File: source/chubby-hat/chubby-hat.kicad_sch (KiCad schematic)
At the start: 29 parts, among them J10 Conn_ARM_JTAG_SWD_10, J11 Conn_ARM_JTAG_SWD_10, J12 TC2030, J13 5V, J14 5V, J15 5V, J16 5V, J9 UART, SW1 RUN, SW2 BOOT, U1 AMS1117-3.3, U2 RP2040-Zero

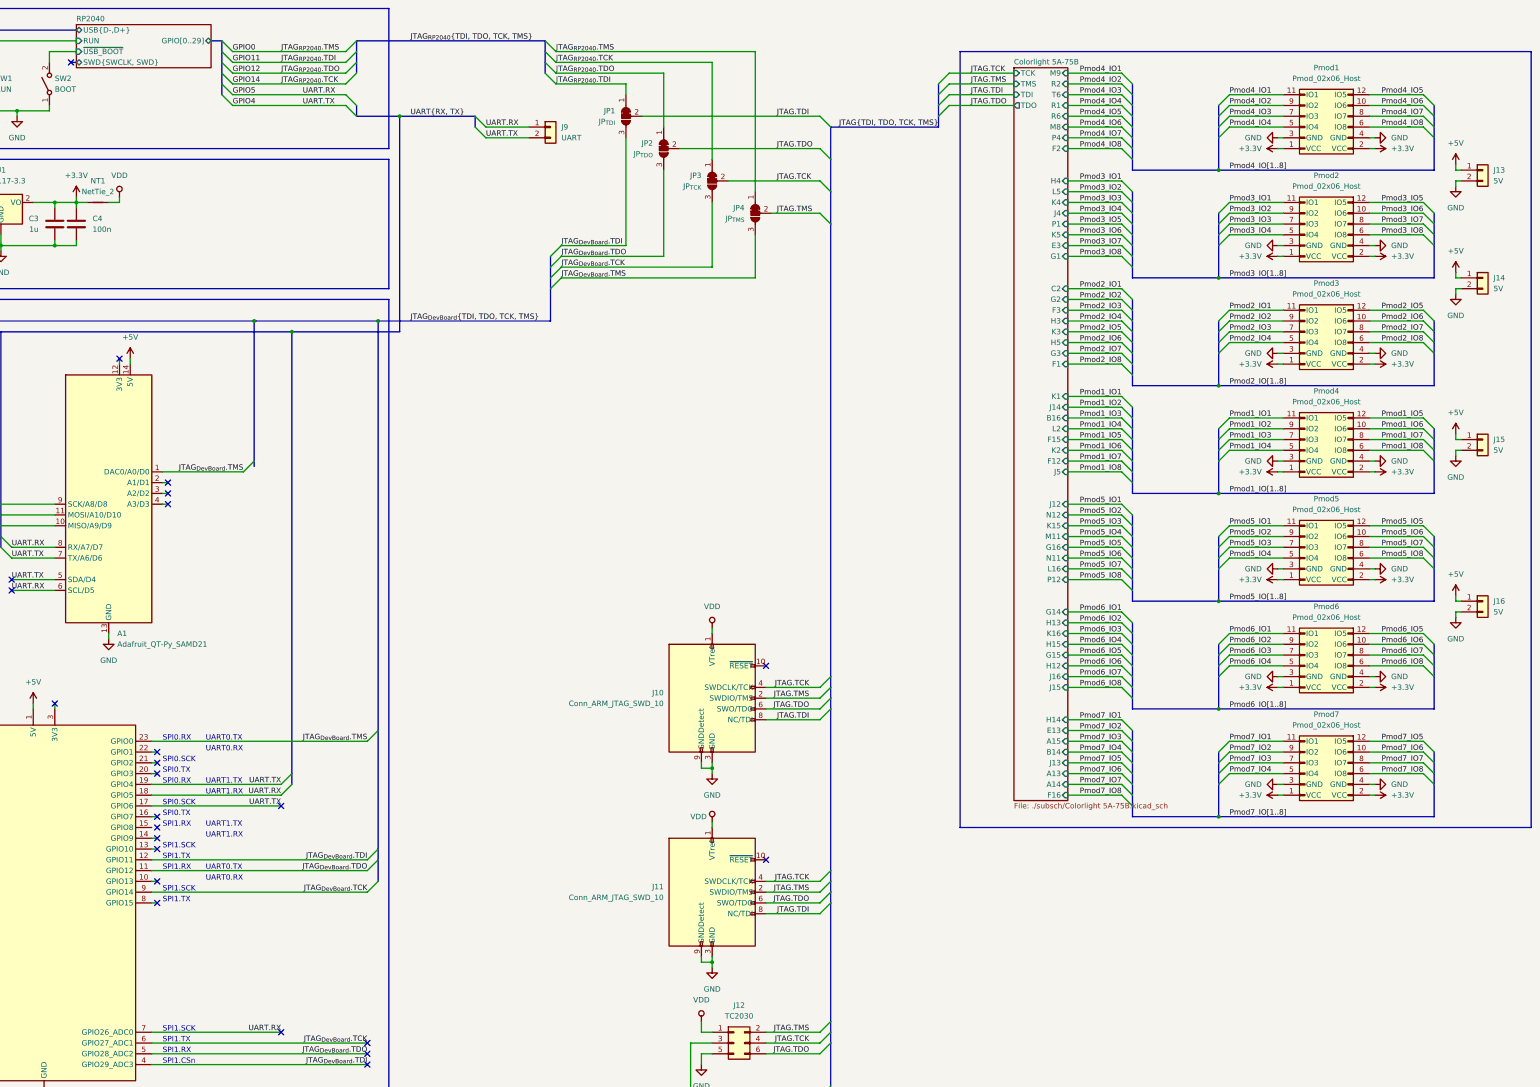
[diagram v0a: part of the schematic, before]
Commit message: added connectors for v8.0; improved power layout
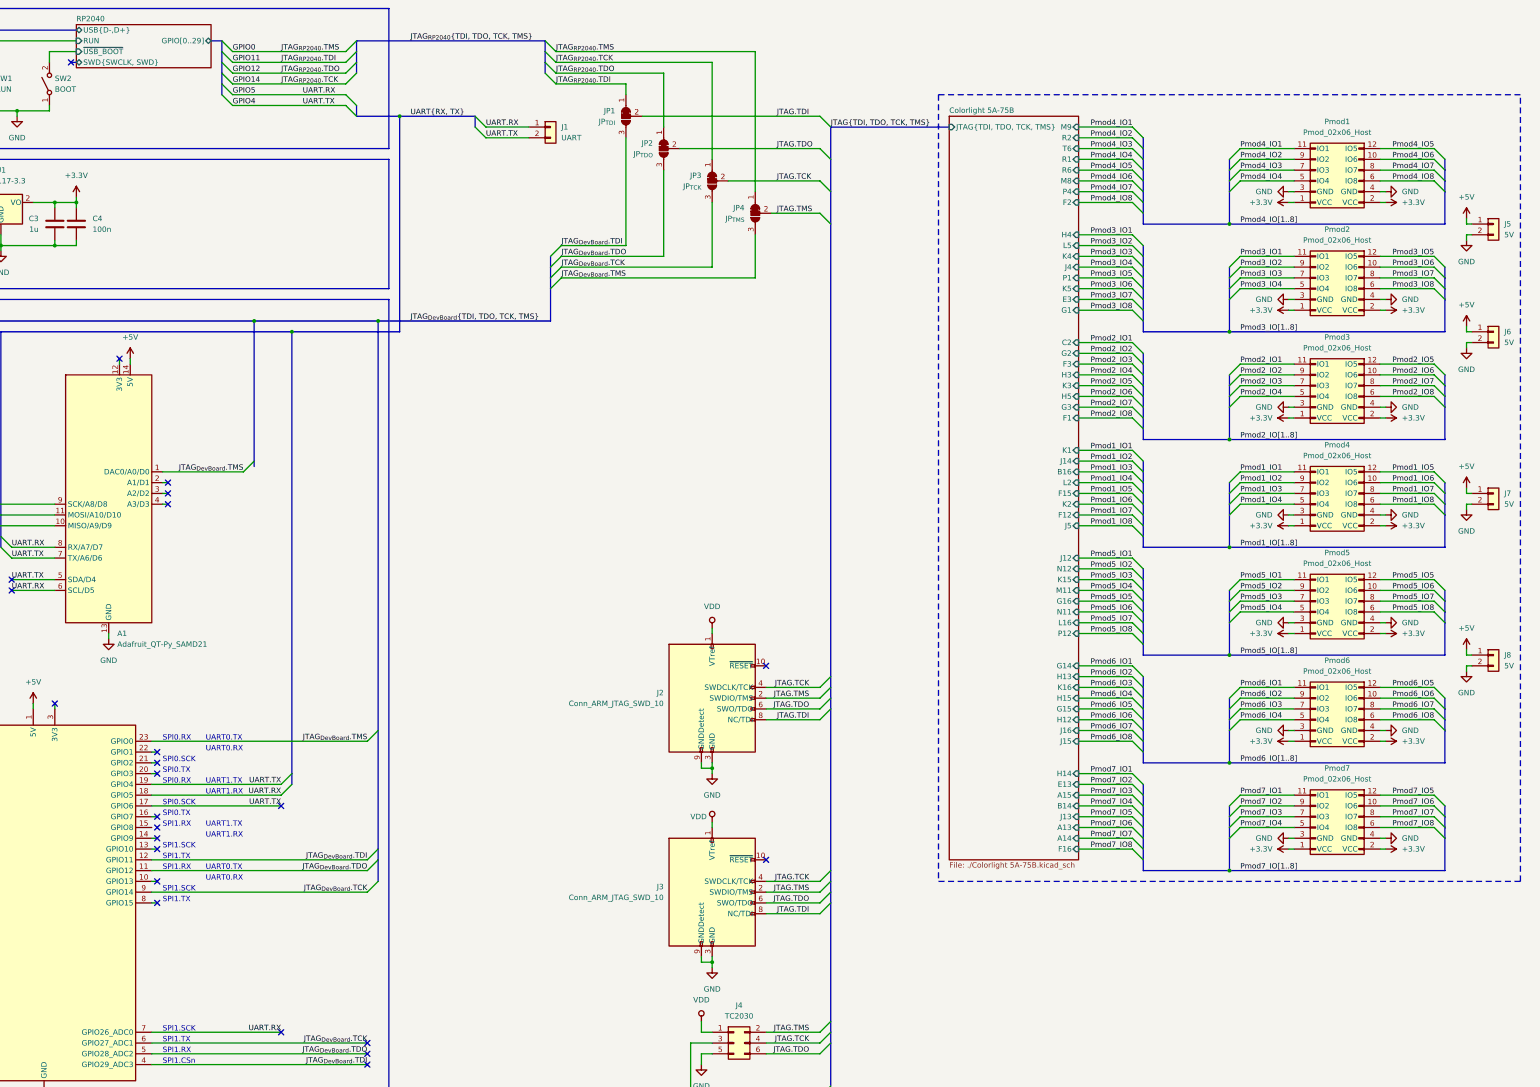
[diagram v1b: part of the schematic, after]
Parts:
- removed NT1: NetTie_2, NetTie:NetTie-2_SMD_Pad0.5mm, symbol Device:NetTie_2
- renumbered J9 to J1, J10 to J2, J11 to J3, J12 to J4, J13 to J5, J14 to J6, J15 to J7, J16 to J8
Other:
- sheet Colorlight 5A-75B: file ./subsch/Colorlight 5A-75B.kicad_sch -> ./Colorlight 5A-75B.kicad_sch
- sheet Colorlight 5A-75B ports: added JTAG{TDI, TDO, TCK, TMS}; removed TCK, TDI, TDO, TMS
- moved on the sheet: J5, J6, J7, J8, Pmod1, Pmod2, Pmod3, Pmod4, Pmod5, Pmod6, Pmod7

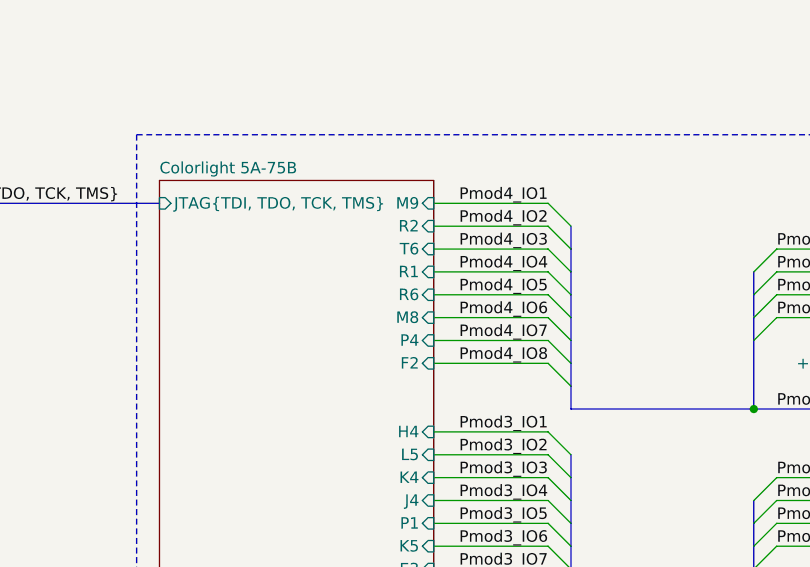
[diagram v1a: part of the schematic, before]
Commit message: switch P4 and R2 on HUB75 J4; closes #5
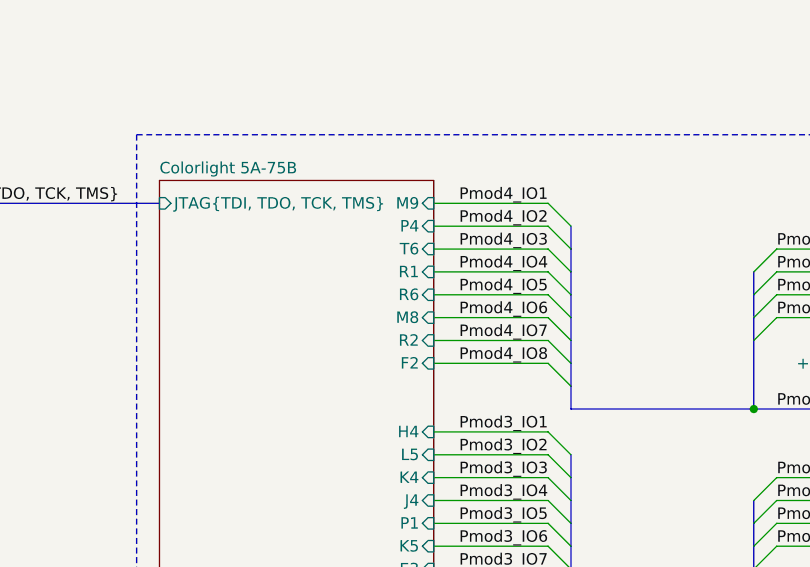
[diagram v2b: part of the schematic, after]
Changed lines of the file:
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@@
       (effects (font (size 1.27 1.27)) (justify right))
     )
-    (pin "P4" input (at 297.18 58.42 0)
+    (pin "P4" input (at 297.18 45.72 0)
       (effects (font (size 1.27 1.27)) (justify right))
     )
@@
       (effects (font (size 1.27 1.27)) (justify right))
     )
-    (pin "R2" input (at 297.18 45.72 0)
+    (pin "R2" input (at 297.18 58.42 0)
       (effects (font (size 1.27 1.27)) (justify right))
     )

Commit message: add test points and leds - closes #1; add fuse - closes #4; add silk screen art
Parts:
- added D1, D2: LED, LED_SMD:LED_0603_1608Metric, symbol Device:LED
- added R1, R2: 1k, Resistor_SMD:R_0603_1608Metric, symbol Device:R
- added TP1: +5V, TestPoint:TestPoint_Pad_D1.0mm, symbol Connector:TestPoint_Small
- added TP10: TCK, TestPoint:TestPoint_Pad_D1.0mm, symbol Connector:TestPoint_Small
- added TP2: +3.3V, TestPoint:TestPoint_Pad_D1.0mm, symbol Connector:TestPoint_Small
- added TP3, TP4, TP5, TP6: GND, TestPoint:TestPoint_Pad_D1.0mm, symbol Connector:TestPoint_Small
- added TP7: TDO, TestPoint:TestPoint_Pad_D1.0mm, symbol Connector:TestPoint_Small
- added TP8: TDI, TestPoint:TestPoint_Pad_D1.0mm, symbol Connector:TestPoint_Small
- added TP9: TMS, TestPoint:TestPoint_Pad_D1.0mm, symbol Connector:TestPoint_Small
- renumbered Pmod7 to Pmod5, Pmod5 to Pmod7
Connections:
- net +3V3: now also D2.2 (A), TP2.1
- net +5V: now also D1.2 (A), TP1.1
- net GND: now also R1.2, R2.2, TP3.1, TP4.1, TP5.1, TP6.1
- net JTAG.TCK: now also TP10.1
- net JTAG.TDI: now also TP8.1
- net JTAG.TDO: now also TP7.1
- net JTAG.TMS: now also TP9.1
- new net: D1.1 (K), R1.1
- new net: D2.1 (K), R2.1
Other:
- moved on the sheet: C2, C3, C4, Pmod5, Pmod7, U1

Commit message: add zero volt diodes to USB and modules; add status LEDs; add RP2040 SWD - closes #9
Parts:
- added D3, D4, D5: LED, LED_SMD:LED_0603_1608Metric, symbol Device:LED
- added J1: RP2040.SWD, Connector_PinHeader_2.54mm:PinHeader_1x03_P2.54mm_Vertical, symbol Connector_Generic:Conn_01x03
- added R3, R4, R5: 5.1k, Resistor_SMD:R_0603_1608Metric, symbol Device:R
- R1, R2: value 1k -> 5.1k
- renumbered J1 to J5, J5 to J6, J6 to J7, J7 to J8, J8 to J9
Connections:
- net +5V: no longer A1.14 (5V), U2.1 (5V)
- net GND: now also J1.1 (Pin_1), R3.2, R4.2, R5.2
- net GPIO3: now reaches U2.20 (GPIO3)
- net GPIO3: now also A1.4 (A3/D3), D5.2 (A)
- net GPIO2: now reaches U2.21 (GPIO2)
- net GPIO2: now also A1.3 (A2/D2), D4.2 (A)
- net GPIO1: now reaches U2.22 (GPIO1)
- net GPIO1: now also A1.2 (A1/D1), D3.2 (A)
- new net: D5.1 (K), R5.1
- new net: D4.1 (K), R4.1
- new net: D3.1 (K), R3.1
- new net +5V_{module}: A1.14 (5V), U2.1 (5V)
- new net SWD.SWCLK: J1.2 (Pin_2)
- new net SWD.SWD: J1.3 (Pin_3)
- no-connect marks 24 -> 17
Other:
- added sheet ZVD2 (ZVD.kicad_sch)
- moved on the sheet: C1, C2, C3, C4, D1, D2, J2, J3, J4, J5, J6, J7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

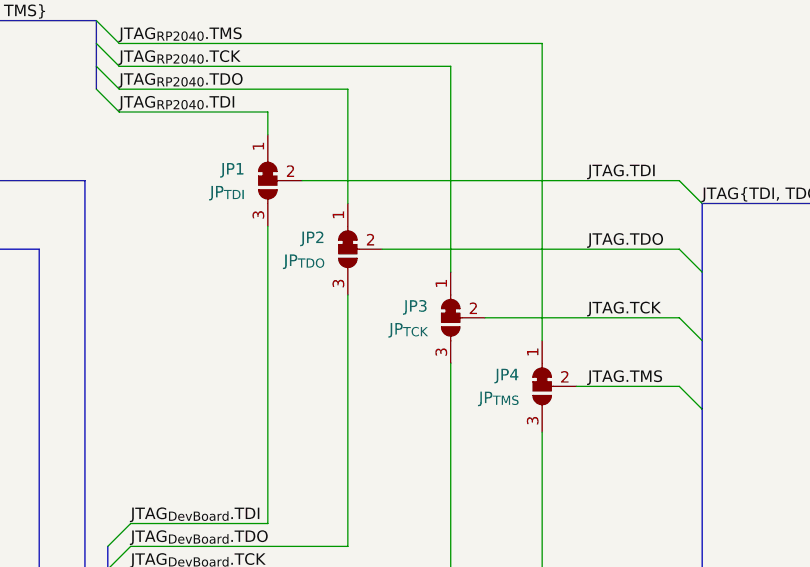
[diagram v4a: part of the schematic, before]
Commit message: moved to KiCad v7.0.0
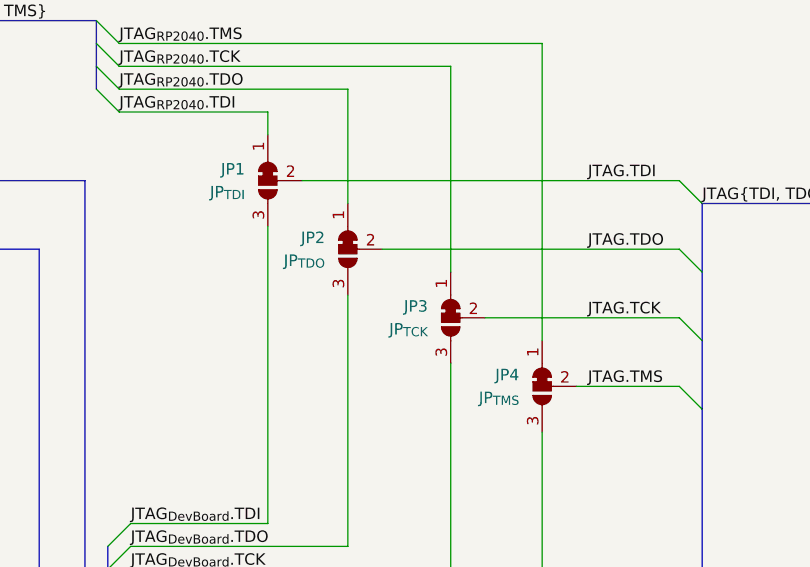
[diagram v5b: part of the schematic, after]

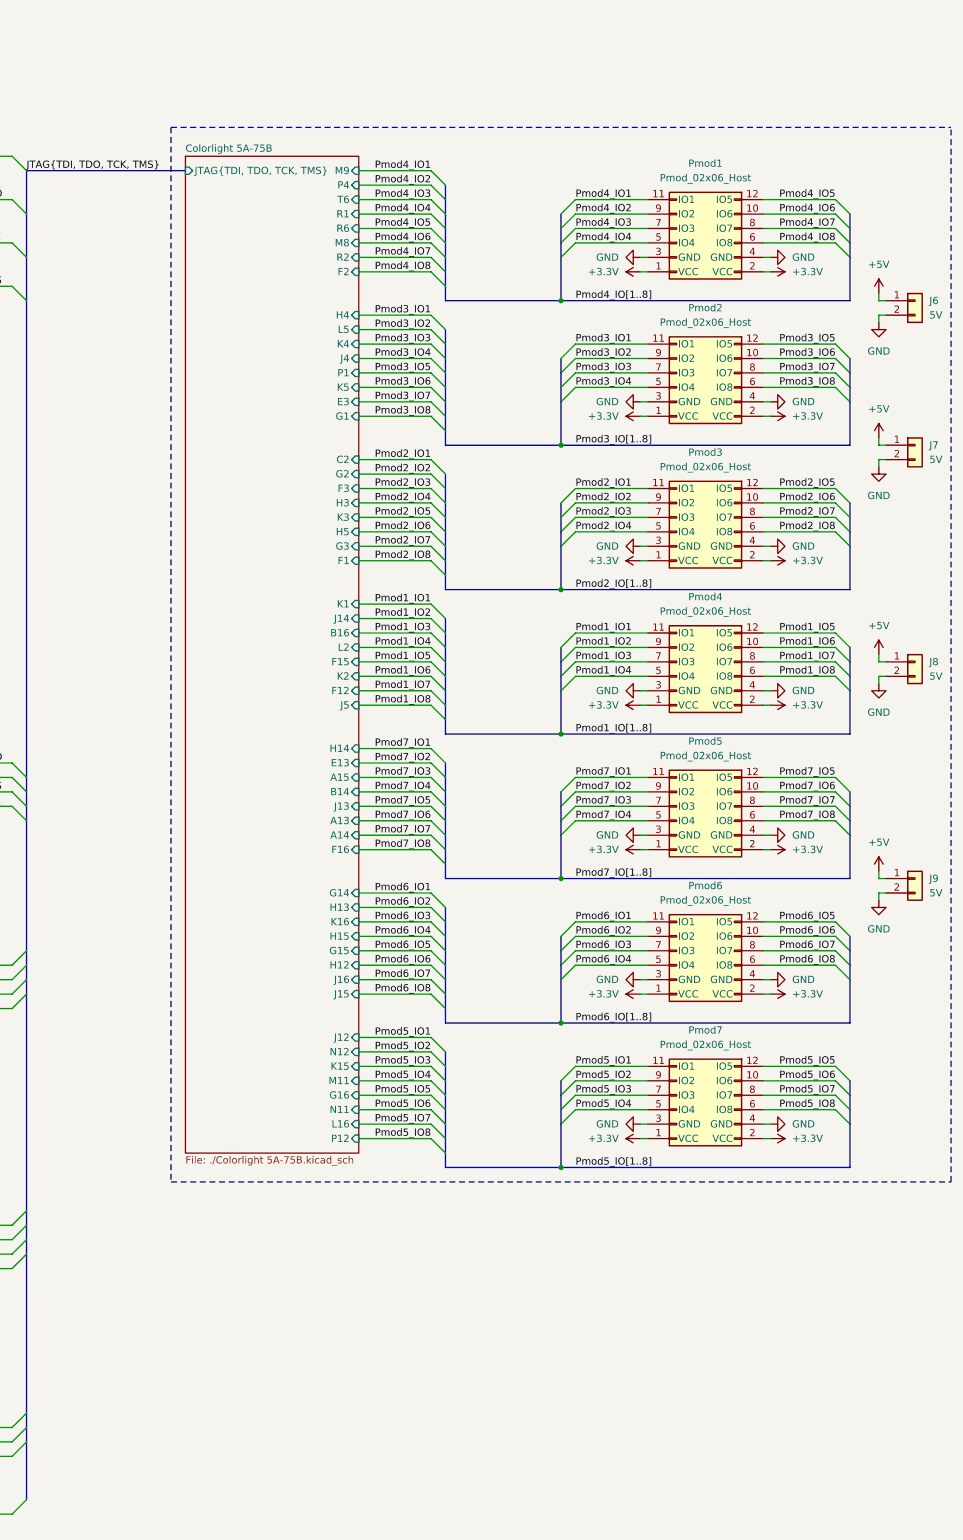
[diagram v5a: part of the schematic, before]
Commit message: add prototyping area; closes #14
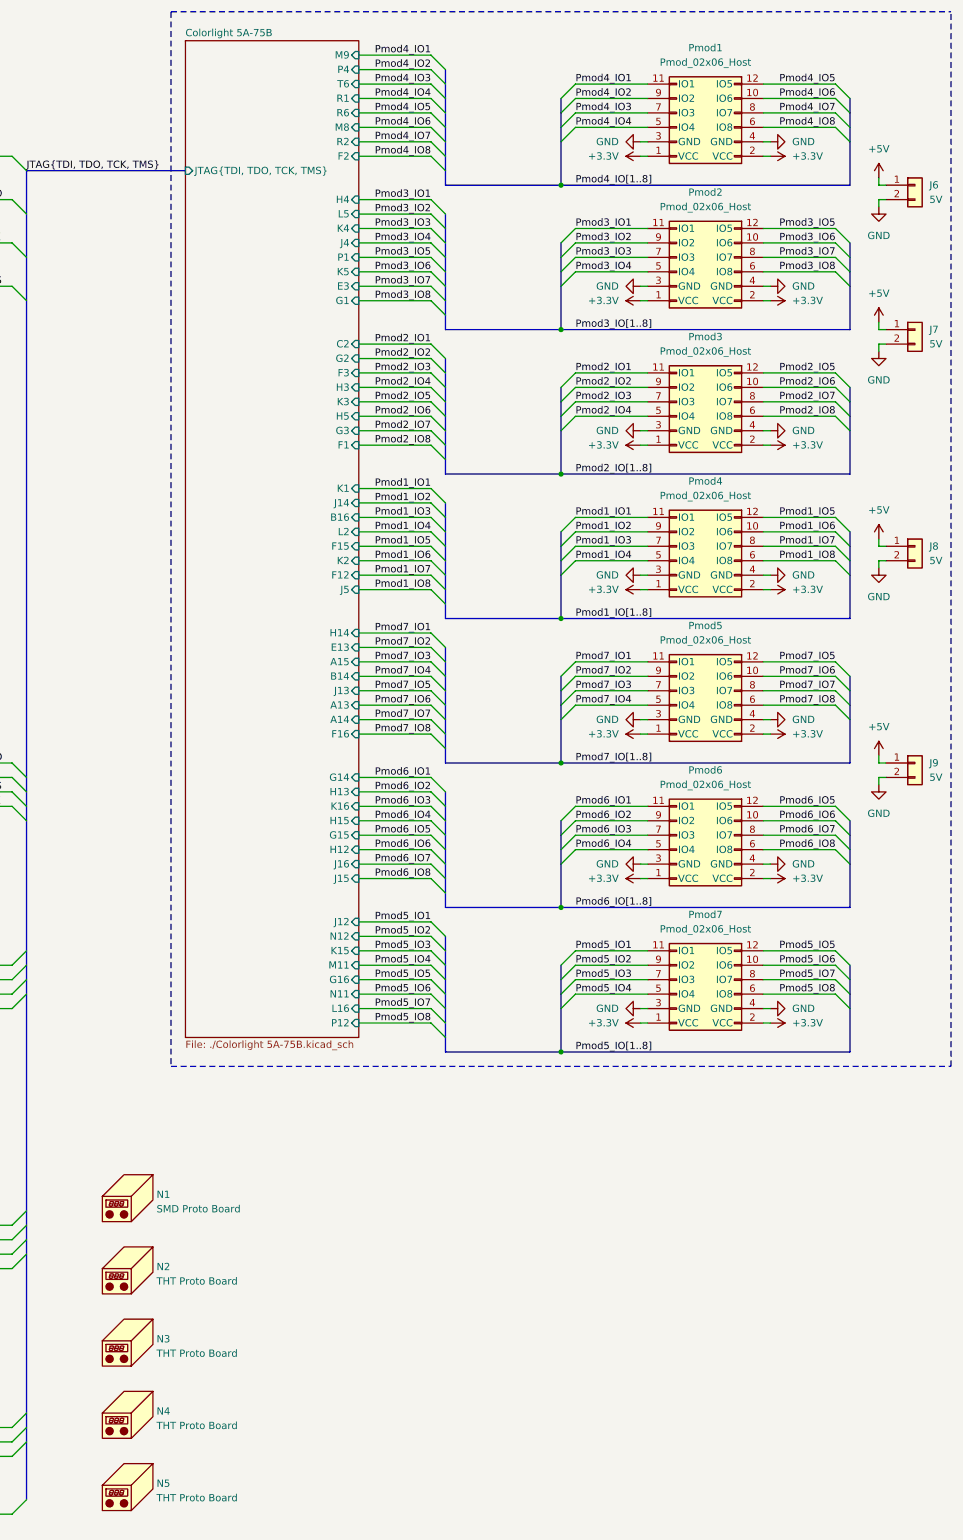
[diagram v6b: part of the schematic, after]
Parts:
- added N1: SMD Proto Board, Prototyping:Proto_SMD_13x17_P1.27mm, symbol Mechanical:Housing
- added N2: THT Proto Board, Prototyping:Proto_THT_07x08_P2.54mm, symbol Mechanical:Housing
- added N3, N4: THT Proto Board, Prototyping:Proto_THT_06x17_P2.54mm, symbol Mechanical:Housing
- added N5: THT Proto Board, Prototyping:Proto_THT_02x15_P2.54mm, symbol Mechanical:Housing
- U1: LCSC (none) -> C5181460; MPN (none) -> AMS1117-3.3
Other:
- moved on the sheet: J6, J7, J8, J9, Pmod1, Pmod2, Pmod3, Pmod4, Pmod5, Pmod6, Pmod7
